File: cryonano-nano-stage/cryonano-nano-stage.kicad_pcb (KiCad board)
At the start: 4 copper layers, 100 x 75 mm, 164 parts, among them J1 24VDC IN, J2 JST-B2B-XH-AM, J3 JST-B2B-XH-AM, J5 JST-B3B-XH-AM, J6 RJ45_Hanrun_HR911105A_Horizon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, J8 Conn_ST_STDC14, J9 USB4930-00-A, Q1 PMV100EPAR, SW1 BOOT, SW2 RESET, U1 AD7124-8BCPZ-RL7, U10 LAN8742A, U11 STM32H753ZITx, U2 NUP4106DR2G, U3 1ED3141MU12FXUMA1, U4 AP7363-33D-13, U5 ECMF02-2AMX6, U6 LP5907MFX-3.3_NOPB, Y3 25.0MHz

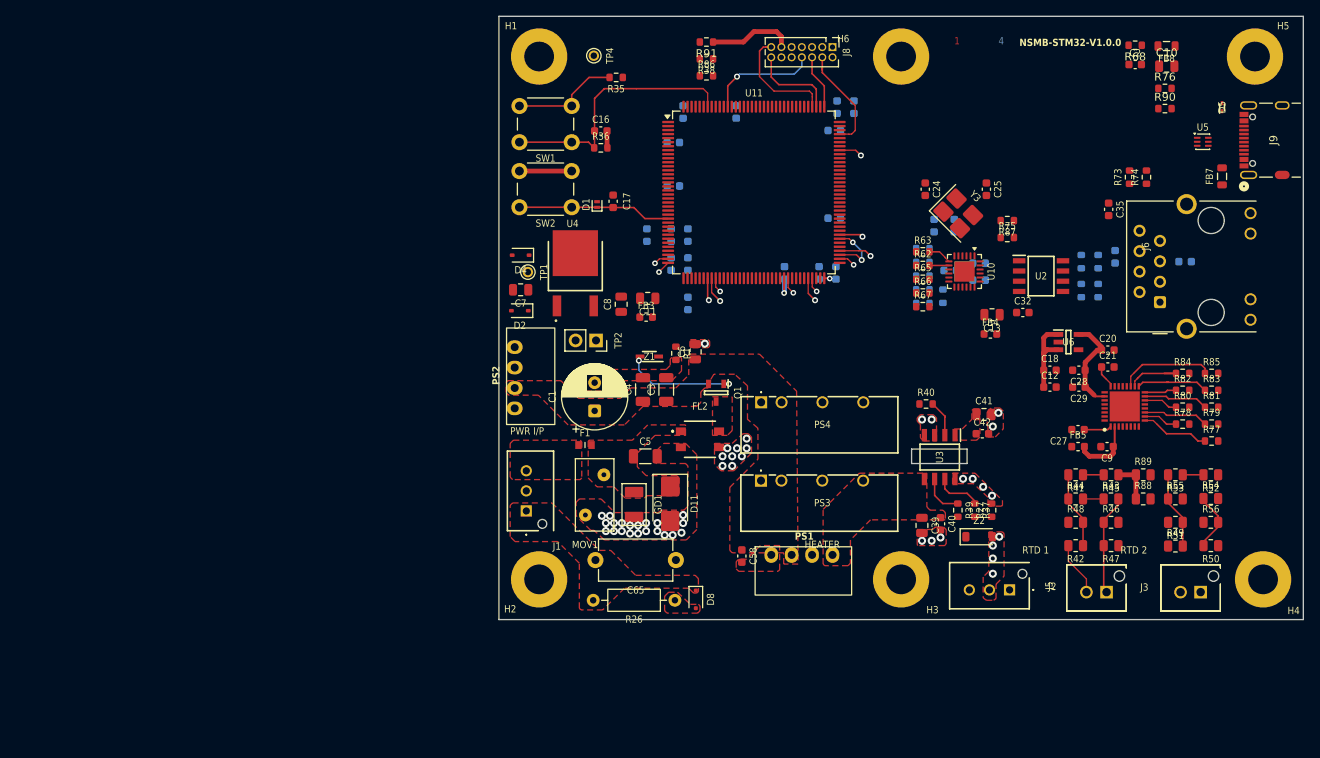
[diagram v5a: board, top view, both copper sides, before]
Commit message: pcb drc ok. 68 ohm matching pending
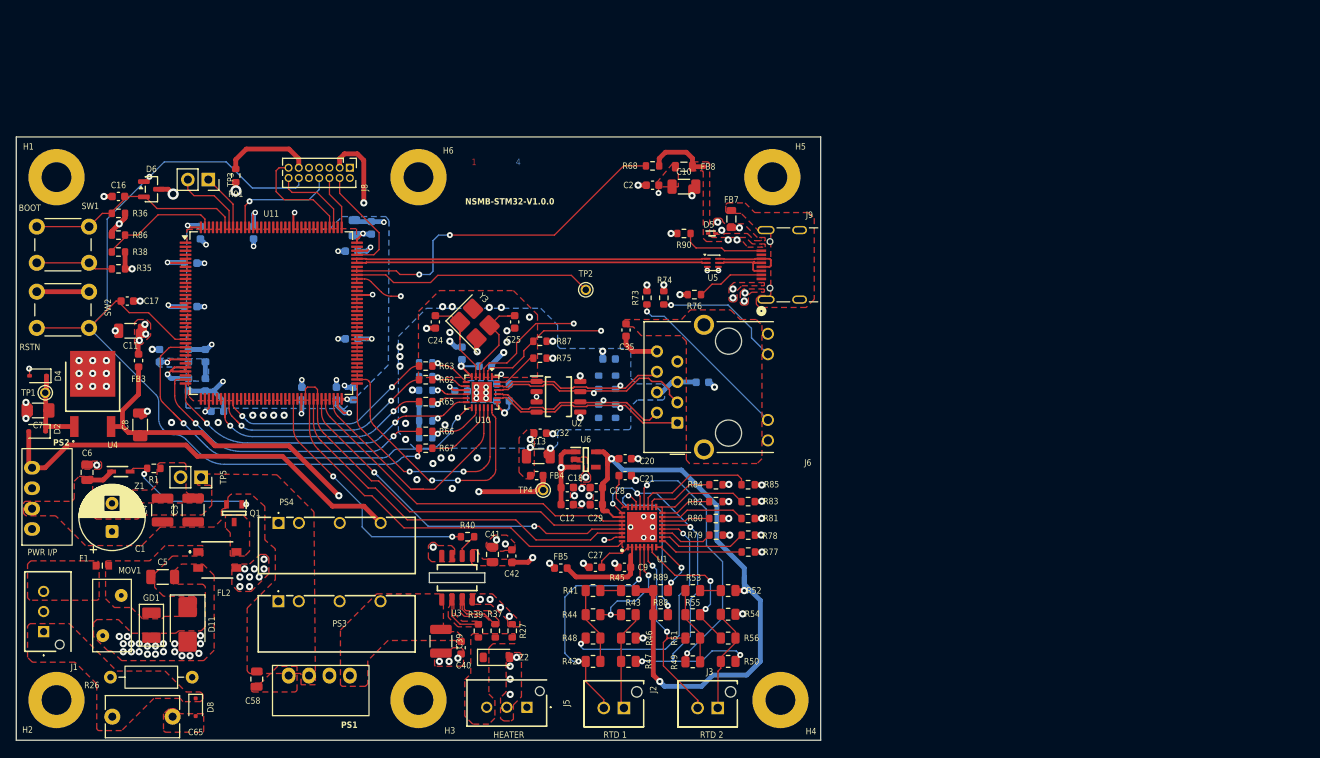
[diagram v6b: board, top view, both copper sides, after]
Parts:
- removed D1: PESD3V3S1UL, Diode_SMD:D_SOD-882
- added D6: ESDB3V3C-AQ, Package_TO_SOT_SMD:SOT-23, F.Cu at (56.8, 71.5)
- added TP3: 1x02 2.54mm, Connector_PinSocket_2.54mm:PinSocket_1x02_P2.54mm_Vertical, F.Cu at (63.9, 70.3)
- added TP5: 1x02 2.54mm, Connector_PinSocket_2.54mm:PinSocket_1x02_P2.54mm_Vertical, F.Cu at (63.0, 107.3)
- C10, C11, C13, C7, C8: footprint Capacitor_SMD:C_0805_2012Metric -> Capacitor_SMD:C_1206_3216Metric
- C14, C58: footprint Capacitor_SMD:C_0603_1608Metric -> Capacitor_SMD:C_0805_2012Metric
- C24, C25: value 5.6p -> 8p
- C3, C4: footprint Capacitor_SMD:C_1206_3216Metric -> Capacitor_SMD:C_1210_3225Metric
- C39: footprint Capacitor_SMD:C_0805_2012Metric -> Capacitor_SMD:C_1210_3225Metric
- C65: footprint Capacitor_THT:C_Disc_D9.0mm_W5.0mm_P10.00mm -> Capacitor_THT:C_Disc_D9.0mm_W5.0mm_P7.50mm
- D5: footprint SamacSys_Parts:SODFL1006X40N -> footprints:SODFL1006X40N
- F1: footprint SamacSys_Parts:FUSC1608X55N -> footprints:FUSC1608X55N
- J2, J3: footprint SamacSys_Parts:B2BXHAMLFSN -> footprints:B2BXHAMLFSN
- TP2: value 24V RAW -> TEST POINT; footprint Connector_PinSocket_2.54mm:PinSocket_1x02_P2.54mm_Vertical -> footprints:TestPoint_THTPad_D1.3mm_Drill0.8mm
- U1: footprint SamacSys_Parts:QFN50P500X500X80-33N-D -> footprints:QFN50P500X500X80-33N-D
- U2, U3: footprint SamacSys_Parts:SOIC127P600X175-8N -> footprints:SOIC127P600X175-8N
- U6: footprint SamacSys_Parts:SOT95P280X145-5N -> footprints:SOT95P280X145-5N
- moved C6 77.1 mm to (48.8, 106.7)
- moved R38 76.9 mm to (52.7, 79.3)
- moved R86 75.7 mm to (52.7, 77.2), turned to 180 degrees
- moved SW1 67.3 mm to (42.5, 76.2), turned to 0 degrees
- moved Z1 67.2 mm to (53.0, 106.6), turned to 0 degrees
- moved R1 66.5 mm to (57.1, 106.2), turned to 0 degrees
- moved R35 66.3 mm to (52.7, 81.4)
- moved R60 66.1 mm to (90.9, 100.3), turned to 0 degrees
- moved FB5 66.0 mm to (107.7, 118.6)
- moved C65 65.5 mm to (59.4, 137.1)
- moved D5 65.3 mm to (126.5, 77.0), turned to 0 degrees
- moved C11 64.4 mm to (54.2, 89.1)
- moved R67 64.3 mm to (90.9, 103.7)
- moved C31 64.2 mm to (113.7, 92.6), turned to 180 degrees
- moved R66 64.1 mm to (90.9, 101.6)
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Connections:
- net /Block Diagram/ADC/A0+ renamed /Block Diagram/ADC/+A0
- net /Block Diagram/ADC/A0- renamed /Block Diagram/ADC/-A0
- net /Block Diagram/ADC/A1+ renamed /Block Diagram/ADC/+A1
- net /Block Diagram/ADC/A1- renamed /Block Diagram/ADC/-A1
- net /Block Diagram/ADC/RTD1_REF+ renamed /Block Diagram/ADC/+REF_RTD1
- net /Block Diagram/ADC/RTD1_REF- renamed /Block Diagram/ADC/-REF_RTD1
- net /Block Diagram/ADC/RTD2_REF+ renamed /Block Diagram/ADC/+REF_RTD2
- net /Block Diagram/Communication/RD_N renamed /Block Diagram/Communication/ETH_RD_N
- net /Block Diagram/Communication/RD_P renamed /Block Diagram/Communication/ETH_RD_P
- net /Block Diagram/Communication/TD_N renamed /Block Diagram/Communication/ETH_TD_N
- net /Block Diagram/Communication/TD_P renamed /Block Diagram/Communication/ETH_TD_P
- net GNDD renamed GND
- net Net-(U10-XTAL1/CLKIN) renamed /Block Diagram/Communication/XTAL1
- net Net-(U10-XTAL2) renamed /Block Diagram/Communication/XTAL2
- TP2 pad 1: /Block Diagram/+24V0 -> /Block Diagram/Controller/MCU GPIO/PA8
- U1 pad 28: /Block Diagram/Controller/MCU GPIO/PB14 -> /Block Diagram/Controller/MCU GPIO/PE10
- U1 pad 29: /Block Diagram/Controller/MCU GPIO/PB15 -> /Block Diagram/Controller/MCU GPIO/PE14
- U1 pad 30: /Block Diagram/Controller/MCU GPIO/PB10 -> /Block Diagram/Controller/MCU GPIO/PE12
- U1 pad 31: /Block Diagram/Controller/MCU GPIO/PA8 -> /Block Diagram/Controller/MCU GPIO/PC9
- U1 pad 32: /Block Diagram/Controller/MCU GPIO/PD11 -> /Block Diagram/Controller/MCU GPIO/PE11
- U10 pad 16: /Block Diagram/Controller/MCU GPIO/PG11 -> /Block Diagram/Controller/MCU GPIO/PB11
- U10 pad 17: /Block Diagram/Controller/MCU GPIO/PG13 -> /Block Diagram/Controller/MCU GPIO/PB12
- U11 pad 103: /Block Diagram/Communication/USB_D+ -> /Block Diagram/Communication/USB_D-
- U11 pad 104: /Block Diagram/Communication/USB_D- -> /Block Diagram/Communication/USB_D+
- U11 pad 66: /Block Diagram/Controller/MCU GPIO/PE13 -> /Block Diagram/Controller/MCU GPIO/PE10
- U11 pad 79: /Block Diagram/Controller/MCU GPIO/PB14 -> /Block Diagram/Controller/MCU GPIO/PD10
- U5 pad 1: /Block Diagram/Communication/USB_D- -> /Block Diagram/Communication/USB_D+
- U5 pad 2: /Block Diagram/Communication/USB_D+ -> /Block Diagram/Communication/USB_D-
- U5 pad 5: /Block Diagram/Communication/D+ -> /Block Diagram/Communication/D-
- U5 pad 6: /Block Diagram/Communication/D- -> /Block Diagram/Communication/D+
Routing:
- net /Block Diagram/+5V0: track 10.1 -> 125.4 mm, vias 0 -> 1
- net V_BUS: track 0.00 -> 103.5 mm, vias 0 -> 2
- net /Block Diagram/Controller/NRST: track 19.1 -> 121.2 mm, vias 0 -> 2
- net /Block Diagram/+3V3: track 0.00 -> 90.0 mm, vias 0 -> 4
- net /Block Diagram/Controller/VDD: track 4.27 -> 77.3 mm, vias 2 -> 18
- net GND: track 8.62 -> 75.1 mm, vias 4 -> 119
- net /Block Diagram/ADC/A+3V3: track 17.7 -> 83.6 mm, vias 0 -> 3
- net /Block Diagram/Controller/MCU GPIO/PC9: track 0.00 -> 59.8 mm, vias 0 -> 2
- net /Block Diagram/Controller/MCU GPIO/PC1: track 0.00 -> 55.4 mm, vias 0 -> 2
- net /Block Diagram/ADC/-REF_RTD1: track 0.00 -> 53.1 mm, vias 0 -> 5
- net /Block Diagram/Power/+5V0: track 0.00 -> 52.6 mm
- net /Block Diagram/Controller/MCU GPIO/PE11: track 0.00 -> 49.7 mm
- net /Block Diagram/Controller/MCU GPIO/PE12: track 0.00 -> 48.3 mm
- net /Block Diagram/Controller/MCU GPIO/PE10: track 2.08 -> 50.4 mm, vias 1 -> 0
- net /Block Diagram/Controller/MCU GPIO/PE14: track 0.00 -> 46.8 mm, vias 0 -> 2
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- added copper zone on B.Cu, net /Block Diagram/Communication/+3V3V
- added copper zone on F.Cu, net /Block Diagram/Communication/+3V3V
- added copper zone on F.Cu, net /Block Diagram/Communication/USB_VBUS
- added copper zone on In2.Cu, net /Block Diagram/Communication/USB_VBUS
- added copper zone on B.Cu, net /Block Diagram/Controller/VDD
- added copper zone on F.Cu, net /Block Diagram/Controller/VDD
- added copper zone on In2.Cu, net /Block Diagram/Controller/VDD
- added copper zone on F.Cu, net /Block Diagram/Heater Drive/SW_G
- added copper zone on B.Cu, net GND
- added copper zone on In1.Cu, net GND
- added copper zone on In2.Cu, net GND
- added copper zone on F.Cu, net Net-(C35-Pad1)
- added copper zone on F.Cu, net Net-(FB7-Pad2)
- added copper zone on F.Cu, net Net-(U3-OUTH)
- added copper zone on F.Cu, net Net-(U3-OUTL)
- added copper zone on F.Cu, net V_BUS
- removed copper zone on In1.Cu, net Net-(FB7-Pad2)
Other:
- outline, holes or cut-outs redrawn
- board text added: "0.185/0.165 100 Ohm +/-10%"
- board text added: "BOOT"
- board text added: "BOT SOLDER MASK Data not available"
- board text added: "DIFFERENTIAL IMPEDENCE"
- board text added: "L1 Outer Cu(TOP) Microstrip/Edge Coupled Microstrip 0.035 L2(GND) 0.215/0.350 50 Ohm +/-10% 0.225/0.165 90 Ohm +/-10%"
- board text added: "L2 GND COPPER 0.035"
- board text added: "L3 GND COPPER 0.035"
- board text added: "L4 Outer Cu(BOT) Microstrip/Edge Coupled Microstrip 0.035 L3(GND) 0.215/0.350 50 Ohm +/-10% 0.225/0.165 90 Ohm +/-10%"
- board text added: "LAYERS"
- board text added: "NP-140 CORE 1.165"
- board text added: "Note: 1. Via has no pad on unconnected layers. 2. Standard buildup as per manufacturer website data. 3. Nominal board thickness: ~1.6 mm; individual layer thicknesses are approximate. 4. Impedance calculations based on εr = 4.3, tanδ = 0.02 at 1 GHz. 5. Impedance values are calculated nominal values and are not impedance-controlled specifications. 6. L1/L4 high-speed signals shall reference the a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"
- board text added: "PREPEG 2116 0.120"
- board text added: "REF. LAYER"
- board text added: "RSTN"
- board text added: "SINGLE ENDED IMPEDENCE"
- board text added: "STACK INFORMATION NOMINAL IMPEDENCE(APPROX.)"
- board text added: "Stack-Up Details(As derived from lioncircuits website data): Layer count = 4 Nominal finished board thickness = 1.6 mm(Approx.) Dielectric model: εr = 4.3, Df/tanδ = 0.02, based on standard FR-4/2116 material data Impedance calculations: 1 GHz nominal"
- board text added: "THICKNESS (mm)"
- board text added: "TOP SOLDER MASK Data not available"
- board text added: "TYPE"
- board text added: "WIDTH/SPACING"

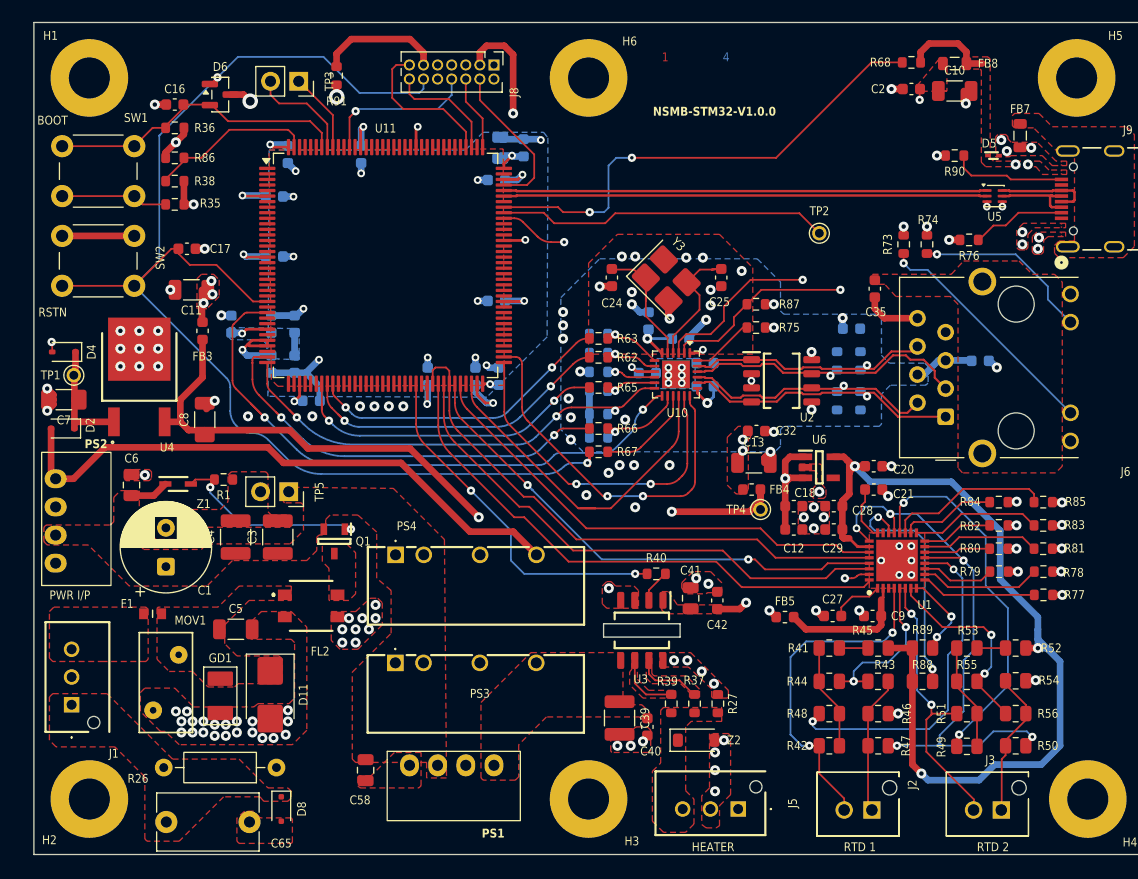
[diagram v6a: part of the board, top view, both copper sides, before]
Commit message: drc no error, only warnings
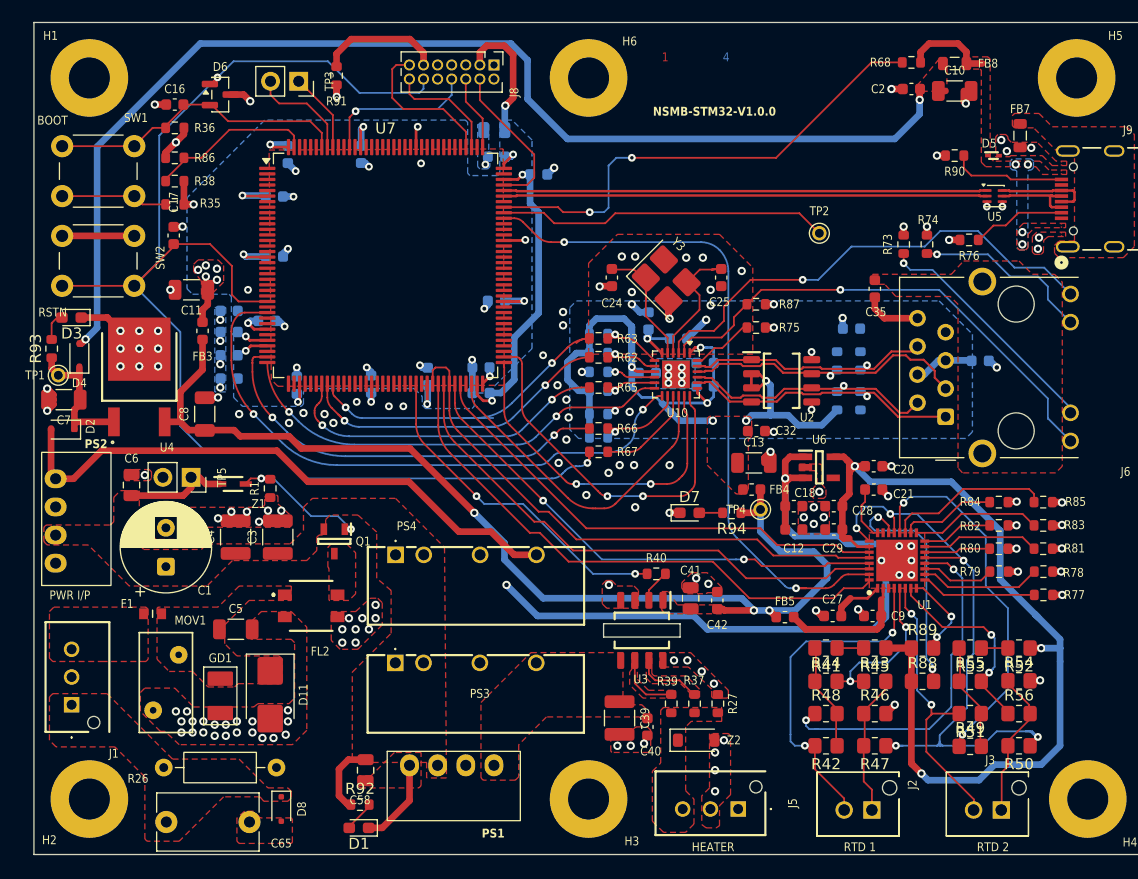
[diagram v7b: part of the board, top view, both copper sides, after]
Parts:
- removed U11: STM32H753ZITx, Package_QFP:LQFP-144_20x20mm_P0.5mm
- added C59: 100n, Capacitor_SMD:C_0603_1608Metric, B.Cu at (70.4, 97.6)
- added D1: LED, LED_SMD:LED_0603_1608Metric_Pad1.05x0.95mm_HandSolder, F.Cu at (69.3, 137.6)
- added D3: LED, LED_SMD:LED_0603_1608Metric_Pad1.05x0.95mm_HandSolder, F.Cu at (43.4, 91.6)
- added D7: LED, LED_SMD:LED_0603_1608Metric_Pad1.05x0.95mm_HandSolder, F.Cu at (99.1, 109.2)
- added R92: 4.7k, Resistor_SMD:R_0603_1608Metric, F.Cu at (69.4, 135.5)
- added R93: 330R, Resistor_SMD:R_0603_1608Metric, F.Cu at (41.6, 94.4)
- added R94: 120R, Resistor_SMD:R_0603_1608Metric, F.Cu at (102.9, 109.2)
- added U7: STM32H753ZITx, Package_QFP:LQFP-144_20x20mm_P0.5mm, F.Cu at (71.7, 86.9)
- R41, R42, R43, R44, R45, R46, R47, R48, R49, R50, R51, R52, R53, R54, R55, R56, R88, R89: footprint Resistor_SMD:R_0805_2012Metric -> Resistor_SMD:R_0805_2012Metric_Pad1.20x1.40mm_HandSolder
- moved TP5 8.90 mm to (54.2, 106.0)
- moved C52 6.04 mm to (57.6, 97.1), turned to 180 degrees
- moved C54 6.02 mm to (57.6, 91.0), turned to 180 degrees
- moved Z1 4.95 mm to (58.0, 106.6)
- moved R1 4.28 mm to (61.3, 107.0), turned to -90 degrees
- moved C53 3.88 mm to (57.6, 95.0), turned to 180 degrees
- moved C55 3.86 mm to (57.6, 92.9), turned to 180 degrees
- moved C57 3.84 mm to (85.5, 78.7), turned to 0 degrees
- moved C43 3.21 mm to (61.0, 91.9), turned to 0 degrees
- moved C49 2.56 mm to (81.7, 77.1), turned to 180 degrees
- moved C44 1.91 mm to (63.7, 97.7), turned to 90 degrees
- moved C48 1.79 mm to (80.3, 96.1), turned to 180 degrees
- moved C17 1.70 mm to (52.6, 84.2), turned to 90 degrees
- moved C14 1.69 mm to (81.5, 74.7), turned to 180 degrees
- moved C56 1.58 mm to (80.3, 98.4), turned to 180 degrees
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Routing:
- net /Block Diagram/Communication/+3V3V: track 18.5 -> 74.3 mm
- net /Block Diagram/Controller/VDD: track 77.3 -> 61.6 mm, vias 18 -> 22
- net /Block Diagram/+24V0: track 3.48 -> 16.0 mm
- net /Block Diagram/+5V0: track 125.4 -> 133.5 mm, vias 1 -> 2
- net /Block Diagram/M24V0: track 0.00 -> 7.88 mm, vias 10 -> 16
- net /Block Diagram/Controller/MCU Power/VCAP: track 33.3 -> 27.6 mm
- net /Block Diagram/+3V3: track 90.0 -> 95.4 mm, vias 4 -> 3
- net /Block Diagram/ADC/-REF_RTD1: track 53.1 -> 58.3 mm
- net Net-(Q1-G): track 17.4 -> 12.5 mm
- net /Block Diagram/Controller/MCU GPIO/PC5: track 27.5 -> 31.2 mm
- net /Block Diagram/Controller/MCU GPIO/PC4: track 29.4 -> 32.8 mm
- net Net-(D1-A): track 0.00 -> 2.85 mm
- net /Block Diagram/ADC/+A0: track 31.2 -> 34.0 mm
- net Net-(D3-A): track 0.00 -> 2.61 mm
- net /Block Diagram/ADC/A+3V3: track 83.6 -> 86.1 mm
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- added copper zone on B.Cu, net /Block Diagram/Communication/USB_VBUS
- removed copper zone on In2.Cu, net /Block Diagram/Communication/USB_VBUS
- removed copper zone on In2.Cu, net /Block Diagram/Controller/VDD
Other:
- board text added: "All dimensions are in mm unless specified otherwise."
- board text removed: "All dimensions are in mm unless othjerwise specified."
